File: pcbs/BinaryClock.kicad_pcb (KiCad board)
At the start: 2 copper layers, 54 parts, among them IC1 ATTINY2313A-S, P1 USB_OTG, P2 CONN_02X03, Q1 DMG9933USD, Q2 DMG9933USD, Q3 DMG9933USD, SW1 SW_PUSH, U1 FT230XS, U2 STP16CPC26, U3 DS3231M

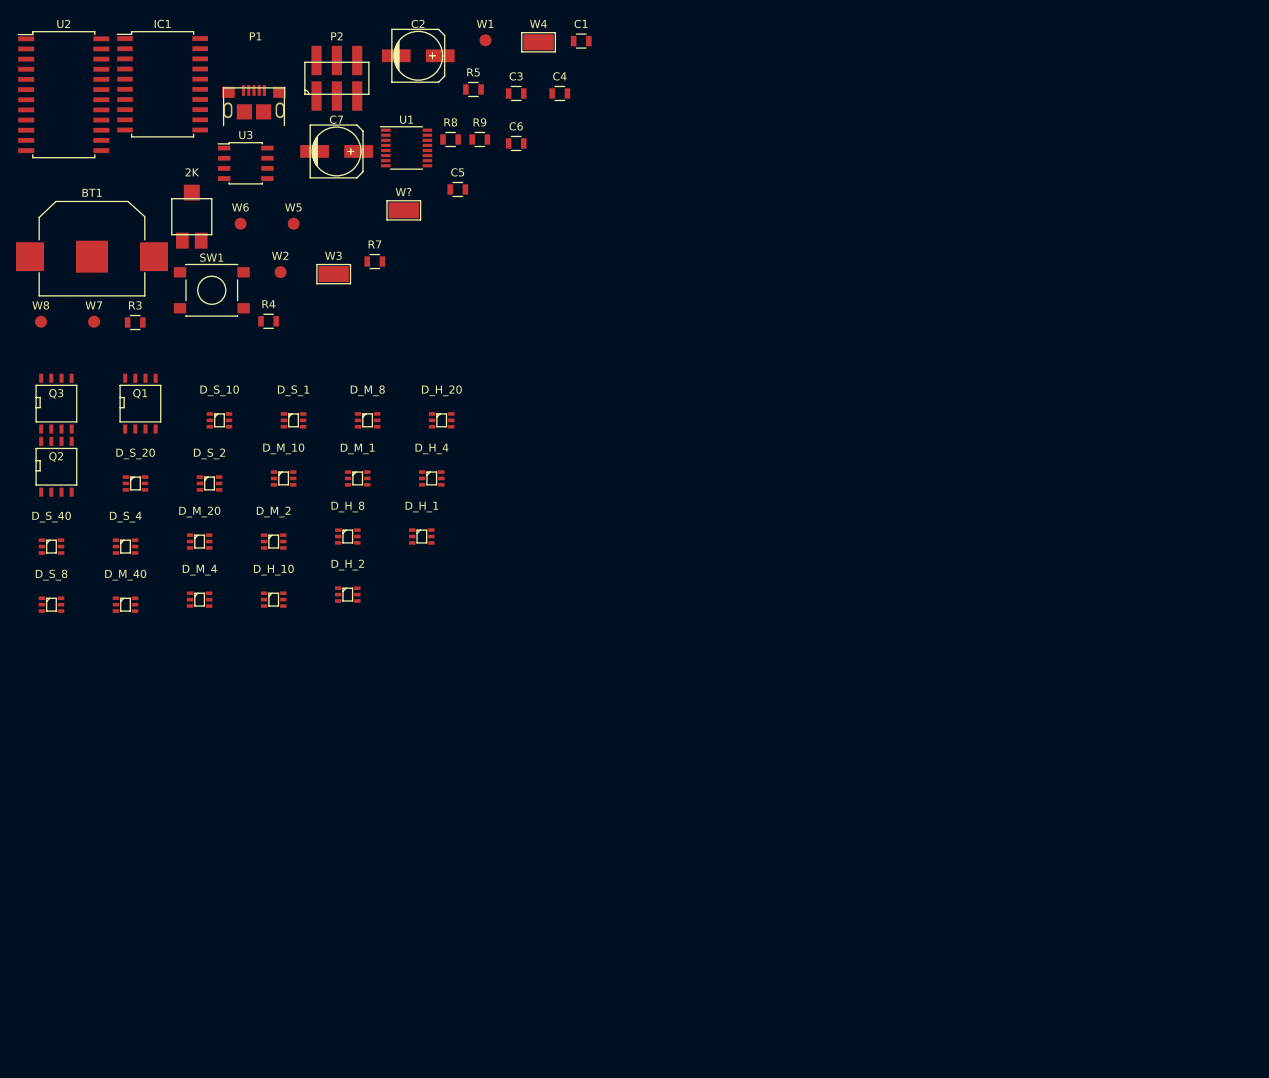
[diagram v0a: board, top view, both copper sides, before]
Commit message: Fixed routing issues, fixed paste layer issues, and eliminated electrolytic caps
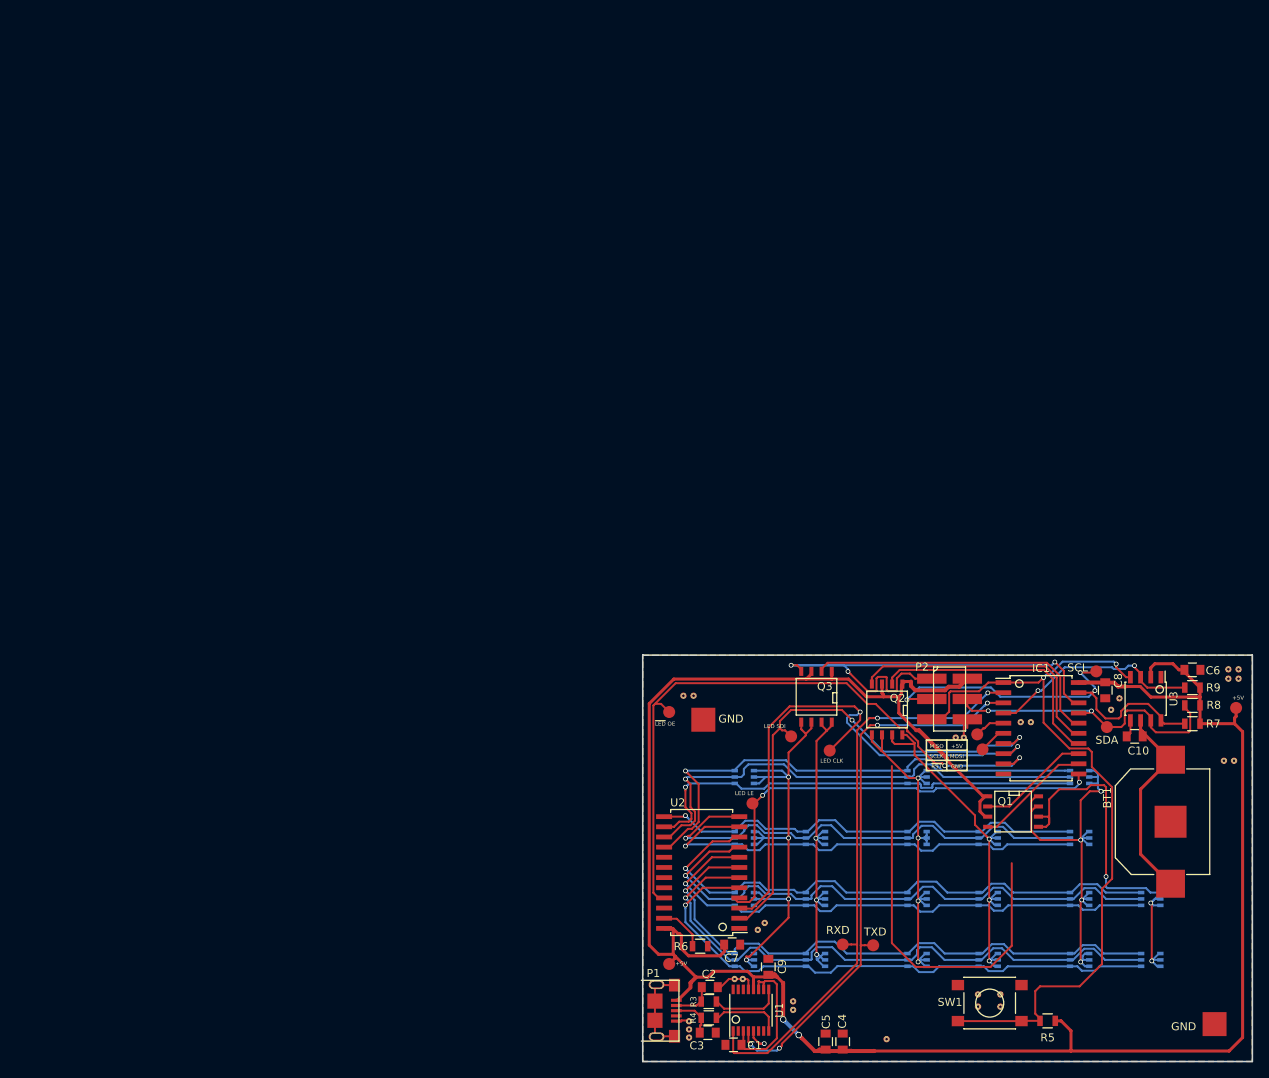
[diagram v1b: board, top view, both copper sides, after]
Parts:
- removed 2K: POT, TylerCustom:pot_trimmer_smd
- removed W?: TEST_1P, Measurement_Points:Test_Point_Keystone_5019_Minature
- added C10: 0.1 uF, Capacitors_SMD:C_0805, F.Cu at (163.1, 111.8)
- added C8: 0.1 uF, Capacitors_SMD:C_0805, F.Cu at (159.4, 106.0)
- added C9: 0.1 uF, Capacitors_SMD:C_0805, F.Cu at (117.3, 140.6)
- added R6: 2K, Resistors_SMD:R_0805, F.Cu at (108.8, 138.0)
- added REF**: via-0.6mm, TylerCustom:via-0.6mm, F.Cu at (176.1, 104.5)
- added REF**: via-0.6mm, TylerCustom:via-0.6mm, F.Cu at (132.1, 149.6)
- added REF**: via-0.6mm, TylerCustom:via-0.6mm, F.Cu at (146.3, 145.5)
- added REF**: via-0.6mm, TylerCustom:via-0.6mm, F.Cu at (143.5, 145.5)
- added REF**: via-0.6mm, TylerCustom:via-0.6mm, F.Cu at (143.5, 144.0)
- added REF**: via-0.6mm, TylerCustom:via-0.6mm, F.Cu at (146.3, 144.0)
- added REF**: via-0.6mm, TylerCustom:via-0.6mm, F.Cu at (106.7, 106.7)
- added REF**: via-0.6mm, TylerCustom:via-0.6mm, F.Cu at (108.0, 106.7)
- added REF**: via-0.6mm, TylerCustom:via-0.6mm, F.Cu at (174.8, 103.4)
- added REF**: via-0.6mm, TylerCustom:via-0.6mm, F.Cu at (176.1, 103.4)
- added REF**: via-0.6mm, TylerCustom:via-0.6mm, F.Cu at (175.5, 114.8)
- added REF**: via-0.6mm, TylerCustom:via-0.6mm, F.Cu at (174.8, 104.5)
- added REF**: via-0.6mm, TylerCustom:via-0.6mm, F.Cu at (174.2, 114.8)
- added REF**: via-0.6mm, TylerCustom:via-0.6mm, F.Cu at (161.2, 107.0)
- added REF**: via-0.6mm, TylerCustom:via-0.6mm, F.Cu at (160.1, 108.4)
- added REF**: via-0.6mm, TylerCustom:via-0.6mm, F.Cu at (148.8, 110.0)
- added REF**: via-0.6mm, TylerCustom:via-0.6mm, F.Cu at (150.1, 110.0)
- added REF**: via-0.6mm, TylerCustom:via-0.6mm, F.Cu at (116.8, 135.1)
- added REF**: via-0.6mm, TylerCustom:via-0.6mm, F.Cu at (116.0, 135.9)
- added REF**: via-0.6mm, TylerCustom:via-0.6mm, F.Cu at (113.1, 142.1)
- added REF**: via-0.6mm, TylerCustom:via-0.6mm, F.Cu at (114.1, 142.1)
- added REF**: via-0.6mm, TylerCustom:via-0.6mm, F.Cu at (140.7, 111.9)
- added REF**: via-0.6mm, TylerCustom:via-0.6mm, F.Cu at (141.7, 111.9)
- added REF**: via-0.6mm, TylerCustom:via-0.6mm, F.Cu at (120.4, 144.9)
- added REF**: via-0.6mm, TylerCustom:via-0.6mm, F.Cu at (120.4, 145.9)
- added REF**: via-0.6mm, TylerCustom:via-0.6mm, F.Cu at (107.4, 149.4)
- added REF**: via-0.6mm, TylerCustom:via-0.6mm, F.Cu at (107.4, 148.4)
- added REF**: via-0.6mm, TylerCustom:via-0.6mm, F.Cu at (107.4, 147.4)
- added W10: TEST_1P, Measurement_Points:Measurement_Point_Round-SMD-Pad_Small, F.Cu at (159.6, 110.6)
- added W11: TEST_1P, Measurement_Points:Measurement_Point_Round-SMD-Pad_Small, F.Cu at (126.6, 137.8)
- added W12: TEST_1P, Measurement_Points:Measurement_Point_Round-SMD-Pad_Small, F.Cu at (130.4, 137.9)
- added W13: TEST_1P, Measurement_Points:Measurement_Point_Round-SMD-Pad_Small, F.Cu at (143.4, 111.5)
- added W14: TEST_1P, Measurement_Points:Measurement_Point_Round-SMD-Pad_Small, F.Cu at (144.1, 113.4)
- added W9: TEST_1P, Measurement_Points:Measurement_Point_Round-SMD-Pad_Small, F.Cu at (158.3, 103.6)
- C1: value 1 uF -> .1 uF; footprint Resistors_SMD:R_0805 -> Capacitors_SMD:C_0805
- C2: value 10 uF -> 47 pF; footprint Capacitors_SMD:c_elec_6.3x5.7 -> Capacitors_SMD:C_0805
- C3: value 0.1 uF -> 47 pF; footprint Resistors_SMD:R_0805 -> Capacitors_SMD:C_0805
- C4: value 0.1 uF -> 1 uF; footprint Resistors_SMD:R_0805 -> Capacitors_SMD:C_0805
- C5: value 0.1 uF -> 4.7 uF; footprint Resistors_SMD:R_0805 -> Capacitors_SMD:C_0805
- C6: footprint Resistors_SMD:R_0805 -> Capacitors_SMD:C_0805
- C7: value 10 uF -> 0.1 uF; footprint Capacitors_SMD:c_elec_6.3x5.7 -> Capacitors_SMD:C_0805
- D_H_1, D_H_10, D_H_2, D_H_20, D_H_4, D_H_8, D_M_1, D_M_10, D_M_2, D_M_20, D_M_4, D_M_40, D_M_8, D_S_1, D_S_10, D_S_2, D_S_20, D_S_4, D_S_40, D_S_8: moved to B.Cu
- W3, W4: footprint Measurement_Points:Test_Point_Keystone_5019_Minature -> Measurement_Points:Measurement_Point_Square-SMD-Pad_Big
- moved BT1 152.2 mm to (167.6, 122.4), turned to 90 degrees
- moved W3 144.6 mm to (173.1, 147.7)
- moved R5 136.8 mm to (152.2, 147.3), turned to 180 degrees
- moved IC1 136.1 mm to (151.4, 110.7)
- moved SW1 131.9 mm to (145.0, 145.1)
- moved U3 130.9 mm to (164.5, 107.1), turned to 270 degrees
- moved C1 126.9 mm to (112.9, 150.3), turned to 180 degrees
- moved U2 125.7 mm to (109.0, 128.8), turned to 180 degrees
- moved W1 125.6 mm to (175.8, 108.2)
- moved C4 123.7 mm to (126.6, 149.9), turned to 90 degrees
- moved P1 123.0 mm to (103.1, 146.1), turned to 270 degrees
- moved C2 122.0 mm to (110.0, 143.1)
- moved Q1 120.4 mm to (147.9, 121.2), turned to 270 degrees
- moved C3 119.8 mm to (109.7, 148.8)
- moved D_H_10 118.5 mm to (165.1, 139.7)
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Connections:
- C1 pad 1: +5V -> Net-(C1-Pad1)
- C2 pad 1: +5V -> Net-(C2-Pad1)
- C3 pad 1: +5V -> Net-(C3-Pad1)
- C7 pad 1: +BATT -> +5V
- P1 pad 2: Net-(P1-Pad2) -> Net-(C2-Pad1)
- P1 pad 3: Net-(P1-Pad3) -> Net-(C3-Pad1)
- R3 pad 1: Net-(P1-Pad2) -> Net-(C2-Pad1)
- R4 pad 1: Net-(P1-Pad3) -> Net-(C3-Pad1)
- U1 pad 1: UART_TXD -> UART_RXD
- U1 pad 10: Net-(U1-Pad10) -> Net-(C1-Pad1)
- U1 pad 11: ~RST -> Net-(C1-Pad1)
- U1 pad 3: Net-(U1-Pad10) -> Net-(C1-Pad1)
- U1 pad 4: UART_RXD -> UART_TXD
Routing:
- net +5V: track 0.00 -> 289.7 mm, vias 0 -> 2
- net ~RST: track 0.00 -> 95.5 mm, vias 0 -> 2
- net ~LEDDRV_OE: track 0.00 -> 81.8 mm, vias 0 -> 2
- net /LED_Sheet/GRE_ONE_CAT: track 0.00 -> 76.4 mm, vias 0 -> 1
- net /LED_Sheet/RED_ONE_CAT: track 0.00 -> 75.1 mm, vias 0 -> 1
- net UART_RXD: track 0.00 -> 74.0 mm, vias 0 -> 2
- net LEDDRV_CLK: track 0.00 -> 73.1 mm, vias 0 -> 2
- net /LED_Sheet/GRE_TWO_CAT: track 0.00 -> 73.0 mm, vias 0 -> 1
- net /LED_Sheet/RED_TWO_CAT: track 0.00 -> 71.8 mm, vias 0 -> 1
- net /LED_Sheet/BLU_ONE_CAT: track 0.00 -> 71.7 mm, vias 0 -> 1
- net UART_TXD: track 0.00 -> 70.3 mm, vias 0 -> 4
- net Net-(D_S_1-Pad4): track 0.00 -> 70.1 mm, vias 0 -> 4
- net /LED_Sheet/BLU_TWO_CAT: track 0.00 -> 69.1 mm, vias 0 -> 1
- net SEC_ONE_ANO: track 0.00 -> 66.1 mm, vias 0 -> 3
- net LEDDRV_SDI: track 0.00 -> 65.6 mm, vias 0 -> 2
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- added copper zone on B.Cu, net GND
- added copper zone on F.Cu, net GND
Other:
- board outline added: 76.2 x 50.8 mm
- net class power added: clearance 0.2, trace_width 0.5, via_dia 0.8, via_drill 0.6
- rule pad_to_mask_clearance: 0 -> 0.2
- rule via_min_size: 0.4 -> 0.3302
- board text added: "+5V"
- board text added: "GND"
- board text added: "LED CLK"
- board text added: "LED LE"
- board text added: "LED SDI"
- board text added: "MISO"
- board text added: "MOSI"
- board text added: "RXD"
- board text added: "SCL"
- board text added: "SCLK"
- board text added: "SDA"
- board text added: "TXD"
- board text added: "~LED OE~"
- board text added: "~RST"
